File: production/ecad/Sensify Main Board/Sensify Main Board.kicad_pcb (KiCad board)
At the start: 4 copper layers, 143 parts, among them J1 1-2834011-3, J2 1-2834011-2, J3 1332645, J4 0532611271, J6 Conn_01x02_Socket, J7 Conn_01x02_Socket, J8 Conn_01x02_Socket, J9 Conn_01x02_Socket, Q1 2N700, Q2 PMPB13XNE,115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

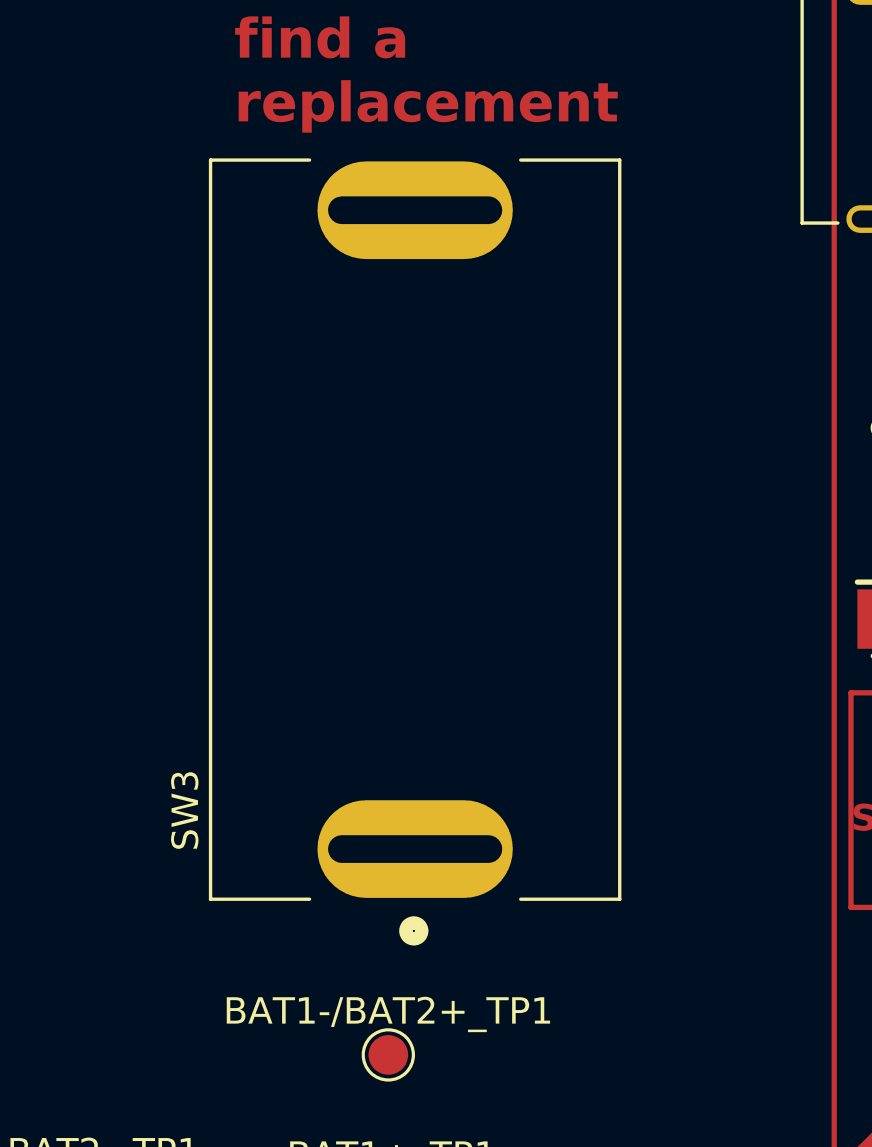
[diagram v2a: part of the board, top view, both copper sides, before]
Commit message: slightly smaller switch added
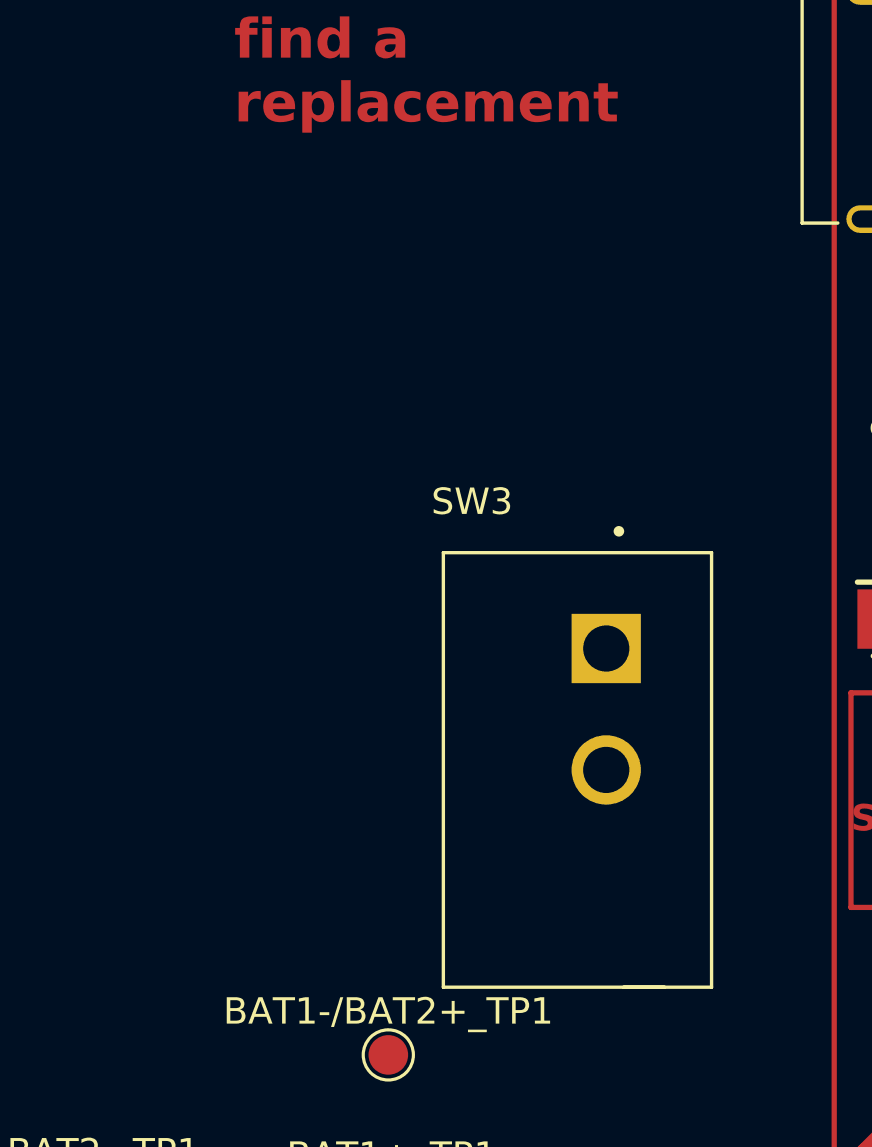
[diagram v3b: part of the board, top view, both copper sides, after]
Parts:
- SW3: value ST141D00 -> SW_GF-123-0054; footprint Sensify Footprints:SW_ST141D00 -> Sensify Footprints:SW_GF-123-0054
- moved SW3 11.0 mm to (117.8, 138.7), turned to -90 degrees
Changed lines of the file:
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@@
     )
   )
-  (footprint "Sensify Footprints:SW_ST141D00" (layer "F.Cu")
-    (at 111.633 129.58135 90)
-    (property "Link" "https://www.digikey.com/en/products/detail/e-switch/ST141D00/2116289")
+  (footprint "Sensify Footprints:SW_GF-123-0054" (layer "F.Cu")
+    (at 117.782 138.684 -90)
     (property "Sheetfile" "BMS.kicad_sch")
     (property "Sheetname" "BMS")
@@
     (property "ki_keywords" "switch lever")
     (attr through_hole)
-    (fp_text reference "SW3" (at -10.63155 -8.69036 90) (layer "F.SilkS")
-        (effects (font (size 1.000614 1.000614) (thickness 0.15)))
+    (fp_text reference "SW3" (at -10.16 3.99) (layer "F.SilkS")
+        (effects (font (size 1 1) (thickness 0.15)))
     )
-    (fp_text value "ST141D00" (at -7.019905 8.621035 90) (layer "F.Fab")
-        (effects (font (size 1.000701 1.000701) (thickness 0.15)))
+    (fp_text value "SW_GF-123-0054" (at 1.27 6.985 90) (layer "F.Fab")
+        (effects (font (size 1 1) (thickness 0.15)))
     )
-    (fp_line (start -14 -7.75) (end 14 -7.75)
+    (fp_line (start -8.23 5.08) (end -8.23 -5.08)
       (stroke (width 0.127) (type solid)) (layer "F.SilkS"))
-    (fp_line (start -14 -4) (end -14 -7.75)
+    (fp_line (start 8.23 -5.08) (end -8.23 -5.08)
       (stroke (width 0.127) (type solid)) (layer "F.SilkS"))
-    (fp_line (start -14 7.75) (end -14 4)
+    (fp_line (start 8.23 -5.08) (end 8.23 5.08)
       (stroke (width 0.127) (type solid)) (layer "F.SilkS"))
-    (fp_line (start 14 -4) (end 14 -7.75)
+    (fp_line (start 8.23 -3.3) (end 8.23 -1.75)
       (stroke (width 0.127) (type solid)) (layer "F.SilkS"))
-    (fp_line (start 14 7.75) (end -14 7.75)
+    (fp_line (start 8.23 5.08) (end -8.23 5.08)
       (stroke (width 0.127) (type solid)) (layer "F.SilkS"))
-    (fp_line (start 14 7.75) (end 14 4)
-      (stroke (width 0.127) (type solid)) (layer "F.SilkS"))
-    (fp_circle (center -15.2 -0.05) (end -14.95 -0.05)
-      (stroke (width 0.6096) (type solid)) (fill none) (layer "F.SilkS"))
-    (fp_line (start -14.25 -8) (end 14.25 -8)
-      (stroke (width 0.127) (type solid)) (layer "F.CrtYd"))
-    (fp_line (start -14.25 8) (end -14.25 -8)
-      (stroke (width 0.127) (type solid)) (layer "F.CrtYd"))
-    (fp_line (start 14.25 -8) (end 14.25 8)
-      (stroke (width 0.127) (type solid)) (layer "F.CrtYd"))
-    (fp_line (start 14.25 8) (end -14.25 8)
-      (stroke (width 0.127) (type solid)) (layer "F.CrtYd"))
-    (fp_line (start -14 7.75) (end -14 -7.75)
+    (fp_circle (center -9.04 -1.57) (end -8.94 -1.57)
+      (stroke (width 0.2) (type solid)) (fill none) (layer "F.SilkS"))
+    (fp_line (start -8.48 -5.33) (end 8.48 -5.33)
+      (stroke (width 0.05) (type solid)) (layer "F.CrtYd"))
+    (fp_line (start -8.48 5.33) (end -8.48 -5.33)
+      (stroke (width 0.05) (type solid)) (layer "F.CrtYd"))
+    (fp_line (start 8.48 -5.33) (end 8.48 5.33)
+      (stroke (width 0.05) (type solid)) (layer "F.CrtYd"))
+    (fp_line (start 8.48 5.33) (end -8.48 5.33)
+      (stroke (width 0.05) (type solid)) (layer "F.CrtYd"))
+    (fp_line (start -8.23 -5.08) (end 8.23 -5.08)
       (stroke (width 0.127) (type solid)) (layer "F.Fab"))
-    (fp_line (start 14 -7.75) (end 14 7.75)
+    (fp_line (start -8.23 5.08) (end -8.23 -5.08)
       (stroke (width 0.127) (type solid)) (layer "F.Fab"))
-    (pad "1" thru_hole oval (at -12.1 0 90) (size 3.7 7.4) (drill oval 1.05 6.6) (layers "*.Cu" "*.Mask")
+    (fp_line (start 8.23 -5.08) (end 8.23 5.08)
+      (stroke (width 0.127) (type solid)) (layer "F.Fab"))
+    (fp_line (start 8.23 5.08) (end -8.23 5.08)
+      (stroke (width 0.127) (type solid)) (layer "F.Fab"))
+    (fp_circle (center -9.04 -1.57) (end -8.94 -1.57)
+      (stroke (width 0.2) (type solid)) (fill none) (layer "F.Fab"))
+    (pad "1" thru_hole rect (at -4.6 -1.09 270) (size 2.625 2.625) (drill 1.75) (layers "*.Cu" "*.Mask")
       (net 20 "PACK+") (pinfunction "A") (pintype "passive") (solder_mask_margin 0.102))
-    (pad "2" thru_hole oval (at 12.1 0 90) (size 3.7 7.4) (drill oval 1.05 6.6) (layers "*.Cu" "*.Mask")
+    (pad "2" thru_hole circle (at 0 -1.09 270) (size 2.625 2.625) (drill 1.75) (layers "*.Cu" "*.Mask")
       (net 23 "Net-(SW3-B)") (pinfunction "B") (pintype "passive") (solder_mask_margin 0.102))
   )

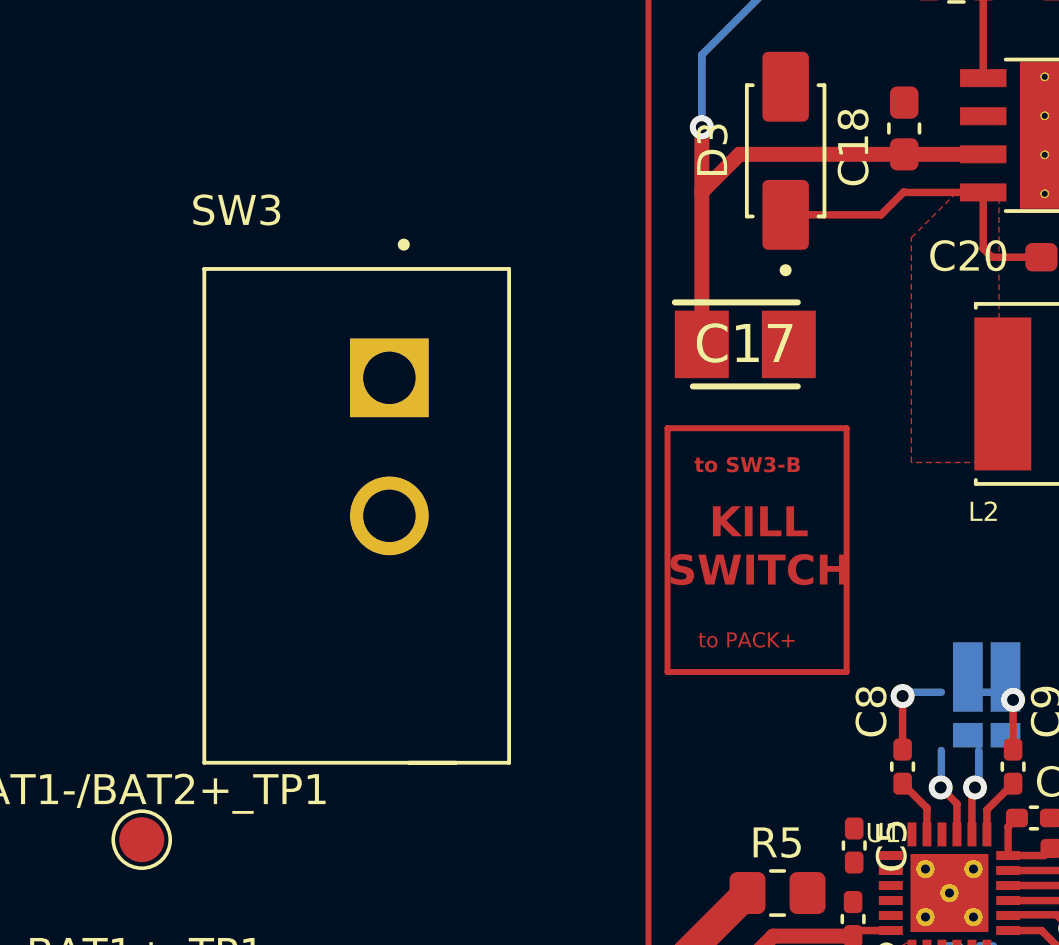
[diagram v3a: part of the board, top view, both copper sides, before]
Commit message: smaller switch
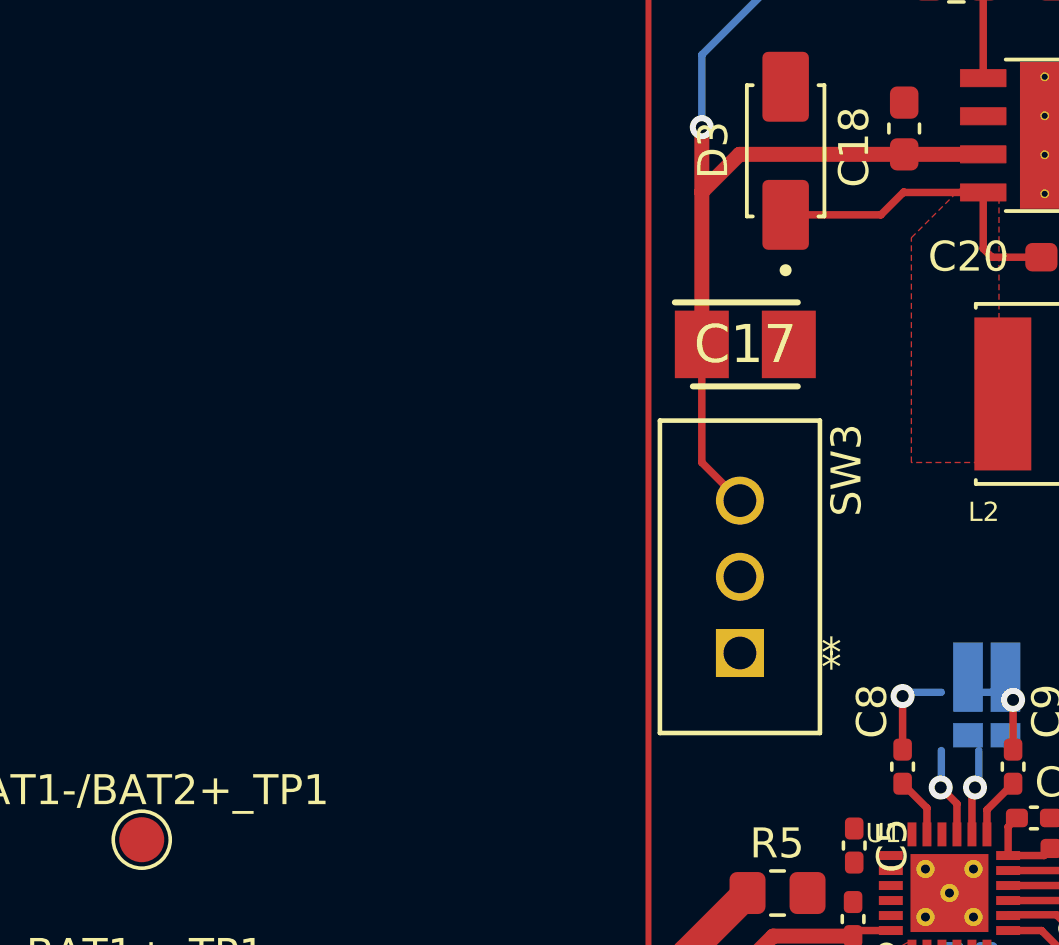
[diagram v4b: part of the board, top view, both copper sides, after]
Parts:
- SW3: value SW_GF-123-0054 -> 500ASSP3M2QE; footprint Sensify Footprints:SW_GF-123-0054 -> Sensify Footprints:500ASSP3M2QE_EWI
- moved SW3 13.6 mm to (130.6, 143.3), turned to 180 degrees
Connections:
- C17 pad 1: Net-(SW3-B) -> Net-(U4-VIN)
- C18 pad 1: Net-(SW3-B) -> Net-(U4-VIN)
- R23 pad 1: Net-(SW3-B) -> Net-(U4-VIN)
- SW3 pad 1: PACK+ -> unconnected-(SW3-Pad1)
- SW3 pad 2: Net-(SW3-B) -> PACK+
- U4 pad 7: Net-(SW3-B) -> Net-(U4-VIN)
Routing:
- net Net-(U4-VIN): track 0.00 -> 33.9 mm, vias 0 -> 2
- net Net-(SW3-B): track 28.2 -> 0.00 mm, vias 2 -> 0
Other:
- board text removed: "KILL SWITCH"
- board text removed: "to PACK+"
- board text removed: "to SW3-B"

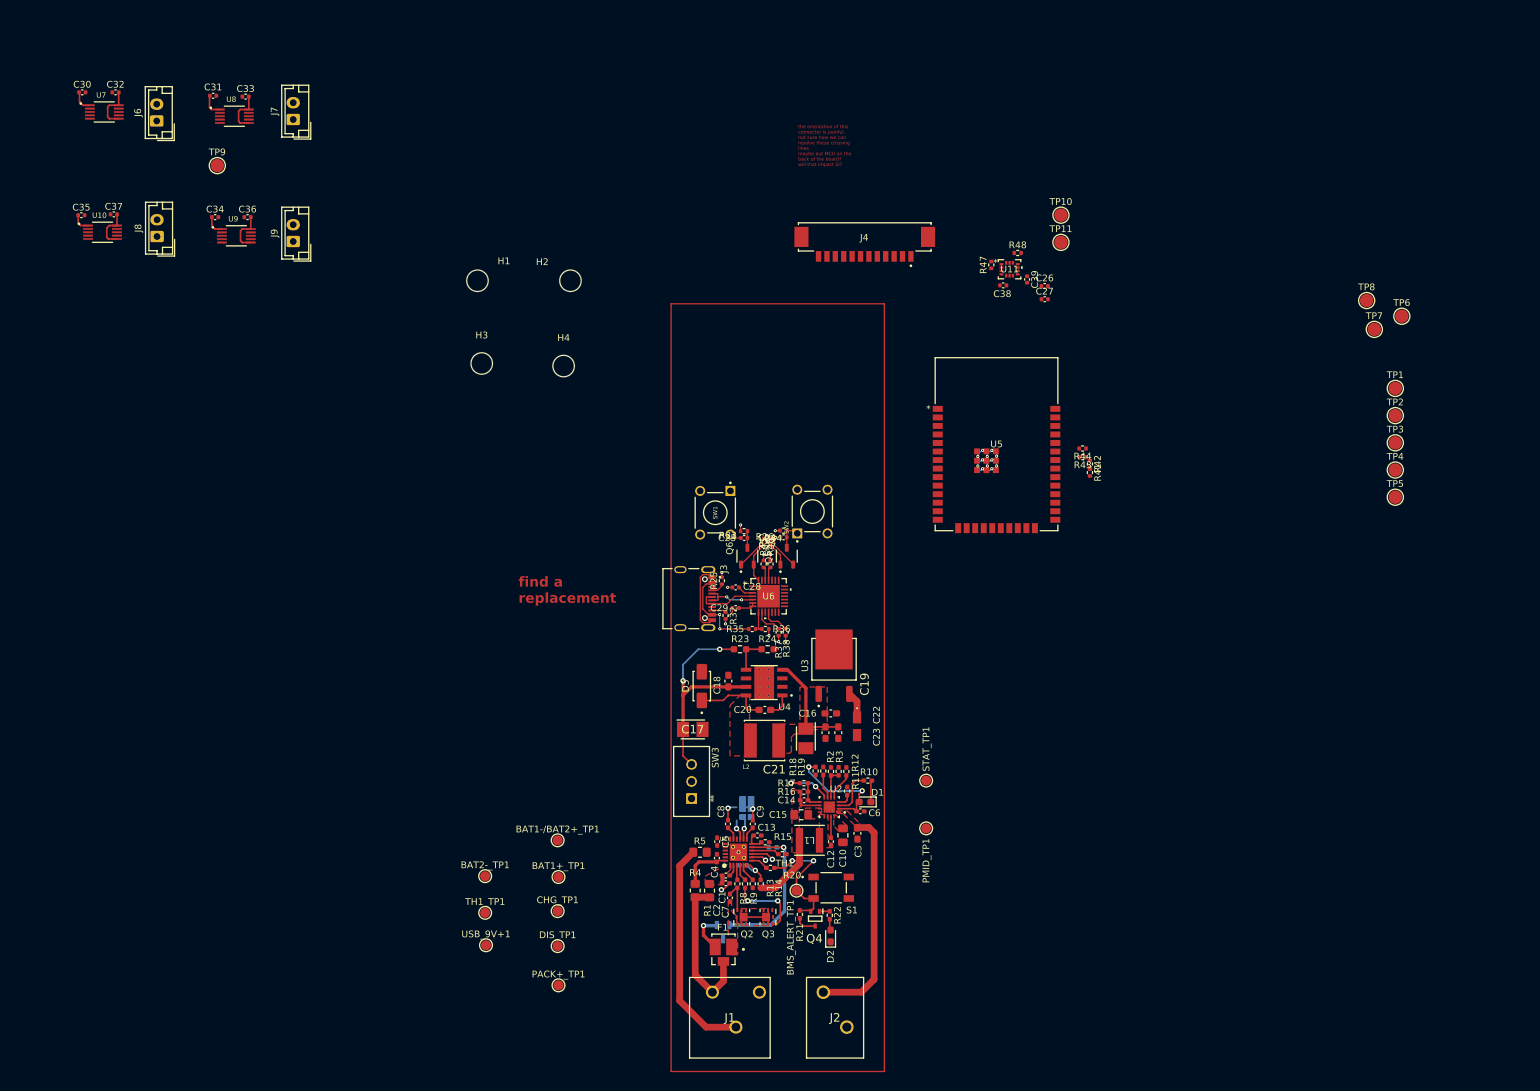
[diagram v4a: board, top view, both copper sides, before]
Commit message: smaller bms alert pushbutton +fixed reference designators + imu and haptics routing + tried to make stuff closer together
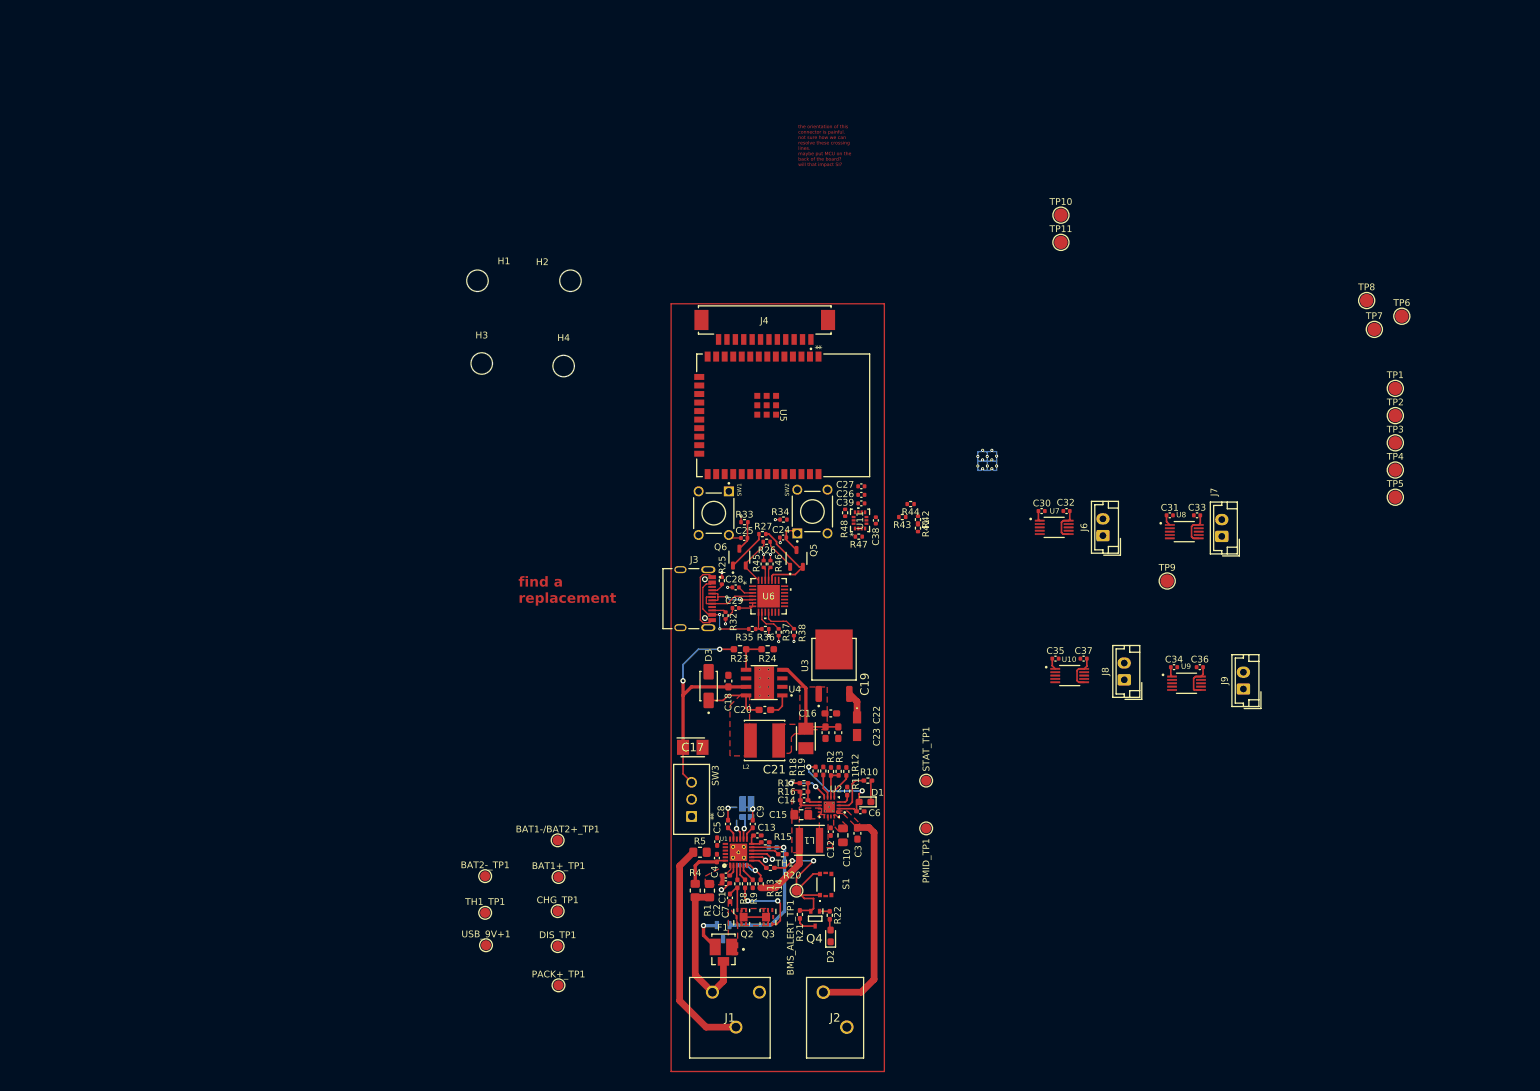
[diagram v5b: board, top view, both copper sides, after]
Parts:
- S1: value PTS_647_SM38_SMTR2_LFS -> 435151014845; footprint Sensify Footprints:SW_PTS_647_SM38_SMTR2_LFS -> Sensify Footprints:435151014845
- moved C35 159.3 mm to (184.7, 122.4)
- moved C37 158.8 mm to (188.9, 122.4)
- moved J8 158.4 mm to (195.0, 125.6)
- moved U10 158.4 mm to (186.9, 124.9)
- moved C34 157.7 mm to (202.4, 123.7)
- moved C36 156.8 mm to (206.2, 123.7)
- moved J9 156.4 mm to (212.7, 126.9)
- moved U9 156.4 mm to (204.2, 126.1)
- moved C30 155.8 mm to (182.7, 100.5)
- moved C31 155.5 mm to (201.8, 101.1)
- moved C33 154.8 mm to (205.8, 101.1)
- moved C32 154.7 mm to (186.4, 100.5)
- moved TP9 154.4 mm to (201.4, 110.9)
- moved U7 154.4 mm to (184.5, 102.9)
- moved U8 154.4 mm to (203.9, 103.5)
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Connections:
- S1 pad 1: GND -> BMS_ALERT
- S1 pad 2: (no net) -> BMS_ALERT
- S1 pad 3: BMS_ALERT -> GND
- S1 pad 4: (no net) -> GND
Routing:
- net RTS: track 5.27 -> 13.6 mm
- net BMS_ALERT: track 18.5 -> 26.8 mm
- net +5V: track 42.2 -> 37.3 mm
- net Net-(U2-BTST): track 3.17 -> 0.00 mm
- net Net-(U4-VIN): track 33.9 -> 36.6 mm
- net IO0: track 2.50 -> 4.48 mm
- net Net-(U8-REG): track 3.46 -> 1.63 mm
- net Net-(U7-REG): track 3.17 -> 1.51 mm
- net Net-(U9-REG): track 3.00 -> 1.47 mm
- net DTR: track 6.12 -> 7.64 mm
- net Net-(Q5-Pad1): track 3.47 -> 4.93 mm
- net Net-(U6-SUSPENDb): track 4.14 -> 5.37 mm
- net Net-(U10-REG): track 2.82 -> 1.71 mm
- net Net-(U4-SW): track 10.8 -> 9.82 mm
- net Net-(Q6-Pad1): track 5.30 -> 6.29 mm
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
